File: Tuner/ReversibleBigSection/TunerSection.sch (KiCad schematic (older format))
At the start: 121 parts, among them J1 Conn_01x03, J10 Conn_01x02, J11 Conn_02x05_Odd_Even, J12 Conn_01x01, J13 Conn_01x01, J14 Conn_01x01, J15 Conn_01x01, J16 Conn_01x01, J17 Conn_01x01, J18 Conn_01x01, J19 Conn_01x01, J2 Conn_01x03, J20 Conn_01x01, J21 Conn_01x01, J22 Conn_01x01, J23 Conn_01x02, J3 Conn_01x03, J4 Conn_01x03, J5 Conn_01x03, J6 Conn_01x03, J7 Conn_01x03, J8 Conn_01x02, J9 Conn_01x02, P10 Conn_01x01, P11 Conn_01x01, P12 Conn_01x01, P2 Conn_01x01, P3 Conn_01x01, P4 Conn_01x01, P5 Conn_01x01, P6 Conn_01x01, P7 Conn_01x01, P8 Conn_01x01, P9 Conn_01x01, U1 MCP23008, U2 ULN2803A

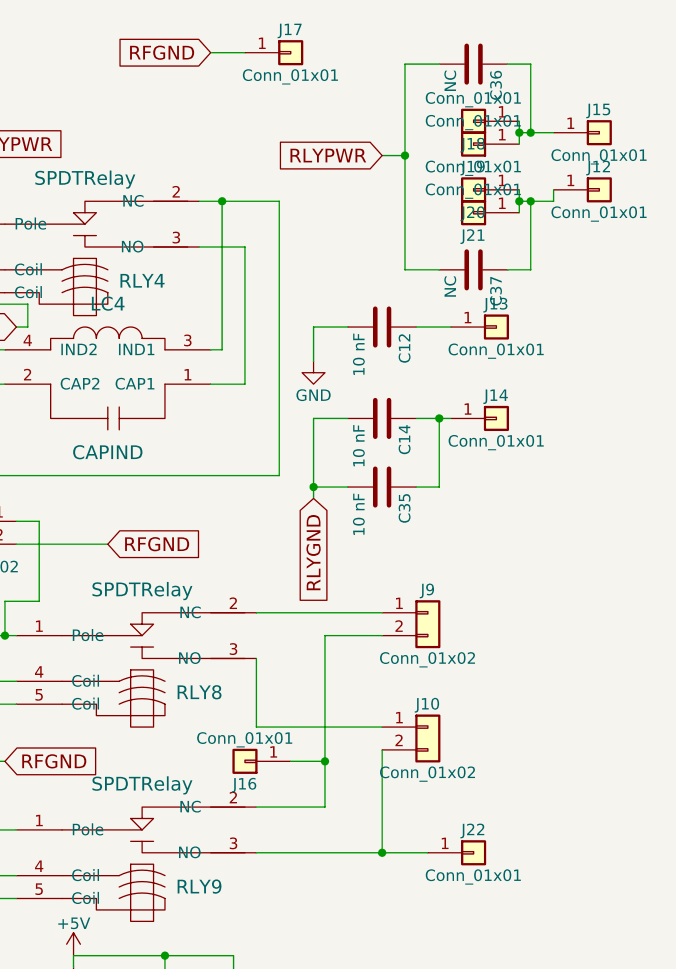
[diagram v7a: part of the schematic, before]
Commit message: Added extra mounting holes to ground ReversibleLittleSection
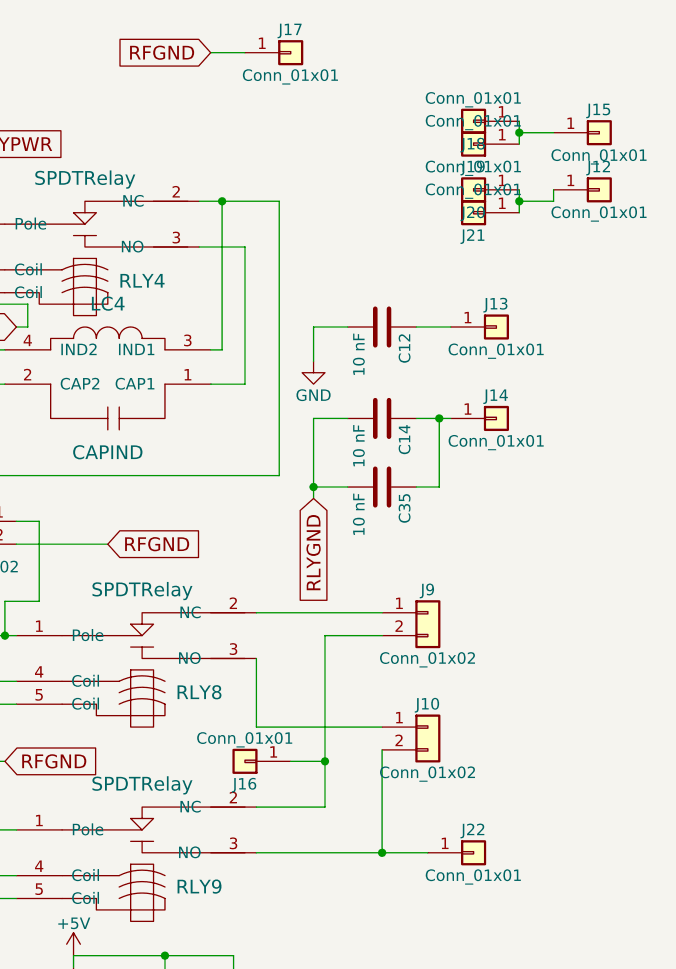
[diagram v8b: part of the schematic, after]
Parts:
- removed C36, C37: NC, Capacitors_THT:C_Disc_D5.0mm_W2.5mm_P2.50mm, symbol C
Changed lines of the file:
@@
 RLY8
 $Comp
-L +5V #PWR12
+L +5V #PWR01
 U 1 1 5B1A0287
 P 3150 5750
-F 0 "#PWR12" H 3150 5600 50  0001 C CNN
+F 0 "#PWR01" H 3150 5600 50  0001 C CNN
 F 1 "+5V" H 3150 5890 50  0000 C CNN
 F 2 "" H 3150 5750 50  0001 C CNN
@@
 $EndComp
 $Comp
-L GND #PWR3
+L GND #PWR02
 U 1 1 5B1AA0F6
 P 900 4500
-F 0 "#PWR3" H 900 4250 50  0001 C CNN
+F 0 "#PWR02" H 900 4250 50  0001 C CNN
 F 1 "GND" H 900 4350 50  0000 C CNN
 F 2 "" H 900 4500 50  0001 C CNN
@@
 $EndComp
 $Comp
-L +5V #PWR2
+L +5V #PWR03
 U 1 1 5B1AABE9
 P 900 3750
-F 0 "#PWR2" H 900 3600 50  0001 C CNN
+F 0 "#PWR03" H 900 3600 50  0001 C CNN
 F 1 "+5V" H 900 3890 50  0000 C CNN
 F 2 "" H 900 3750 50  0001 C CNN
@@
 $EndComp
 $Comp
-L +5V #PWR8
+L +5V #PWR04
 U 1 1 5B1ABA5A
 P 2150 4450
-F 0 "#PWR8" H 2150 4300 50  0001 C CNN
+F 0 "#PWR04" H 2150 4300 50  0001 C CNN
 F 1 "+5V" H 2150 4590 50  0000 C CNN
 F 2 "" H 2150 4450 50  0001 C CNN
@@
 $EndComp
 $Comp
-L +5V #PWR10
+L +5V #PWR05
 U 1 1 5B1ABCDE
 P 2400 3950
-F 0 "#PWR10" H 2400 3800 50  0001 C CNN
+F 0 "#PWR05" H 2400 3800 50  0001 C CNN
 F 1 "+5V" H 2400 4090 50  0000 C CNN
 F 2 "" H 2400 3950 50  0001 C CNN
@@
 $EndComp
 $Comp
-L +5V #PWR16
+L +5V #PWR06
 U 1 1 5B1ABFC6
 P 8800 4600
-F 0 "#PWR16" H 8800 4450 50  0001 C CNN
+F 0 "#PWR06" H 8800 4450 50  0001 C CNN
 F 1 "+5V" H 8800 4740 50  0000 C CNN
 F 2 "" H 8800 4600 50  0001 C CNN
@@
 $EndComp
 $Comp
-L GND #PWR17
+L GND #PWR07
 U 1 1 5B1AC04C
 P 8800 5050
-F 0 "#PWR17" H 8800 4800 50  0001 C CNN
+F 0 "#PWR07" H 8800 4800 50  0001 C CNN
 F 1 "GND" H 8800 4900 50  0000 C CNN
 F 2 "" H 8800 5050 50  0001 C CNN
@@
 $EndComp
 $Comp
-L +5V #PWR9
+L +5V #PWR08
 U 1 1 5B196BCE
 P 2250 3950
-F 0 "#PWR9" H 2250 3800 50  0001 C CNN
+F 0 "#PWR08" H 2250 3800 50  0001 C CNN
 F 1 "+5V" H 2250 4090 50  0000 C CNN
 F 2 "" H 2250 3950 50  0001 C CNN
@@
 $EndComp
 $Comp
-L GND #PWR14
+L GND #PWR09
 U 1 1 5B9A4AE1
 P 4850 6650
-F 0 "#PWR14" H 4850 6400 50  0001 C CNN
+F 0 "#PWR09" H 4850 6400 50  0001 C CNN
 F 1 "GND" H 4850 6500 50  0000 C CNN
 F 2 "" H 4850 6650 50  0001 C CNN
@@
 $EndComp
 $Comp
-L GND #PWR11
+L GND #PWR010
 U 1 1 5B9A6036
 P 3150 4200
-F 0 "#PWR11" H 3150 3950 50  0001 C CNN
+F 0 "#PWR010" H 3150 3950 50  0001 C CNN
 F 1 "GND" H 3150 4050 50  0000 C CNN
 F 2 "" H 3150 4200 50  0001 C CNN
@@
 $EndComp
 $Comp
-L GND #PWR13
+L GND #PWR011
 U 1 1 5B9ACA36
 P 3550 6100
-F 0 "#PWR13" H 3550 5850 50  0001 C CNN
+F 0 "#PWR011" H 3550 5850 50  0001 C CNN
 F 1 "GND" H 3550 5950 50  0000 C CNN
 F 2 "" H 3550 6100 50  0001 C CNN
@@
 $EndComp
 $Comp
-L GND #PWR18
+L GND #PWR012
 U 1 1 5B982525
 P 9850 2000
-F 0 "#PWR18" H 9850 1750 50  0001 C CNN
+F 0 "#PWR012" H 9850 1750 50  0001 C CNN
 F 1 "GND" H 9850 1850 50  0000 C CNN
 F 2 "" H 9850 2000 50  0001 C CNN
@@
 $EndComp
 $Comp
-L GND #PWR7
+L GND #PWR013
 U 1 1 5BA4D8F3
 P 1800 5850
-F 0 "#PWR7" H 1800 5600 50  0001 C CNN
+F 0 "#PWR013" H 1800 5600 50  0001 C CNN
 F 1 "GND" H 1800 5700 50  0000 C CNN
 F 2 "" H 1800 5850 50  0001 C CNN
@@
 $EndComp
 $Comp
-L +5V #PWR6
+L +5V #PWR014
 U 1 1 5BA4E663
 P 1200 5700
-F 0 "#PWR6" H 1200 5550 50  0001 C CNN
+F 0 "#PWR014" H 1200 5550 50  0001 C CNN
 F 1 "+5V" H 1200 5840 50  0000 C CNN
 F 2 "" H 1200 5700 50  0001 C CNN
@@
 $EndComp
 $Comp
-L GND #PWR1
+L GND #PWR015
 U 1 1 5BA4FB25
 P 750 5900
-F 0 "#PWR1" H 750 5650 50  0001 C CNN
+F 0 "#PWR015" H 750 5650 50  0001 C CNN
 F 1 "GND" H 750 5750 50  0000 C CNN
 F 2 "" H 750 5900 50  0001 C CNN
@@
 $EndComp
 $Comp
-L GND #PWR5
+L GND #PWR016
 U 1 1 5BA5005D
 P 1100 5300
-F 0 "#PWR5" H 1100 5050 50  0001 C CNN
+F 0 "#PWR016" H 1100 5050 50  0001 C CNN
 F 1 "GND" H 1100 5150 50  0000 C CNN
 F 2 "" H 1100 5300 50  0001 C CNN
@@
 EXTPWR
 $Comp
-L +5V #PWR4
+L +5V #PWR017
 U 1 1 5BAE4DBC
 P 1000 4850
-F 0 "#PWR4" H 1000 4700 50  0001 C CNN
+F 0 "#PWR017" H 1000 4700 50  0001 C CNN
 F 1 "+5V" H 1000 4990 50  0000 C CNN
 F 2 "" H 1000 4850 50  0001 C CNN
@@
 $EndComp
 $Comp
-L GND #PWR15
+L GND #PWR018
 U 1 1 5BAEE216
 P 5050 7250
-F 0 "#PWR15" H 5050 7000 50  0001 C CNN
+F 0 "#PWR018" H 5050 7000 50  0001 C CNN
 F 1 "GND" H 5050 7100 50  0000 C CNN
 F 2 "" H 5050 7250 50  0001 C CNN
@@
 	9900 3200 10150 3200
 Wire Wire Line
-	9900 3950 9900 3200
+	9900 3200 9900 3950
 Wire Wire Line
 	9600 3600 10150 3600
@@
 	9600 3300 9600 3600
 Wire Wire Line
-	9600 3950 9900 3950
+	9900 3950 9600 3950
 Wire Wire Line
 	9600 3100 10150 3100
@@
 	10300 2250 10450 2250
 Wire Wire Line
-	9850 2600 9850 2250
+	9850 2250 9850 2600
 Wire Wire Line
 	9850 2250 10000 2250
@@
 	10750 1250 10750 1350
 Wire Wire Line
-	10900 1250 10900 1300
-Wire Wire Line
-	10900 1300 10750 1300
+	10900 1300 10900 1250
+Wire Wire Line
+	10750 1300 10900 1300
 Connection ~ 10750 1300
 $Comp
@@
 $EndComp
 Connection ~ 8350 3400
-Text GLabel 10150 1100 0    60   Input ~ 0
-RLYPWR
-$Comp
-L C C36
-U 1 1 5DDBD75D
-P 10550 700
-F 0 "C36" H 10575 800 50  0000 L CNN
-F 1 "NC" H 10575 600 50  0000 L CNN
-F 2 "Capacitors_THT:C_Disc_D5.0mm_W2.5mm_P2.50mm" H 10588 550 50  0001 C CNN
-F 3 "" H 10550 700 50  0001 C CNN
-	1    10550 700
-	0    1    1    0
-$EndComp
-Wire Wire Line
-	10150 1100 10250 1100
-Wire Wire Line
-	10250 700  10250 1600
-Wire Wire Line
-	10250 700  10400 700
-Wire Wire Line
-	10700 700  10800 700
-Wire Wire Line
-	10800 700  10800 1000
-Connection ~ 10800 1000
-$Comp
-L C C37
-U 1 1 5DDBDF54
-P 10550 1600
-F 0 "C37" H 10575 1700 50  0000 L CNN
-F 1 "NC" H 10575 1500 50  0000 L CNN
-F 2 "Capacitors_THT:C_Disc_D5.0mm_W2.5mm_P2.50mm" H 10588 1450 50  0001 C CNN
-F 3 "" H 10550 1600 50  0001 C CNN
-	1    10550 1600
-	0    1    1    0
-$EndComp
-Wire Wire Line
-	10250 1600 10400 1600
-Connection ~ 10250 1100
-Wire Wire Line
-	10700 1600 10800 1600
-Wire Wire Line
-	10800 1600 10800 1300
-Connection ~ 10800 1300
 $EndSCHEMATC
